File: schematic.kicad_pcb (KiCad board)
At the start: 2 copper layers, 169.7 x 127.8 mm, 108 parts, among them J3 USB_C_Receptacle_USB2.0_16P

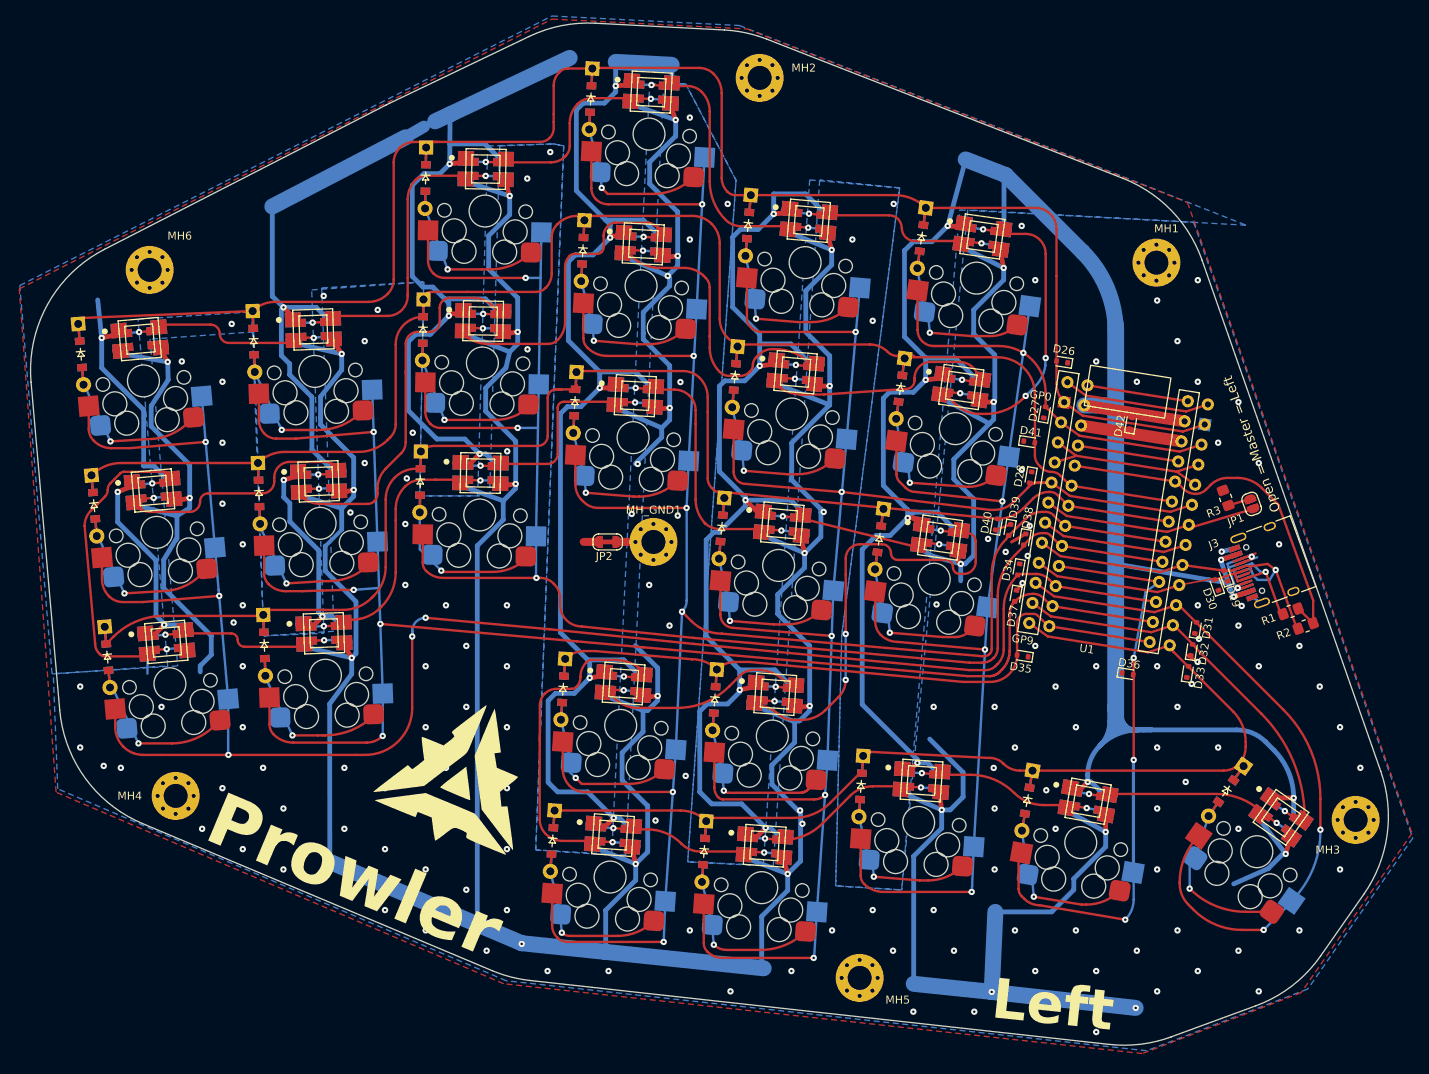
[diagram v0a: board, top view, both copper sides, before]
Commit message: Replace LEDs with reverse mount variant
Previous LEDs collided with switch
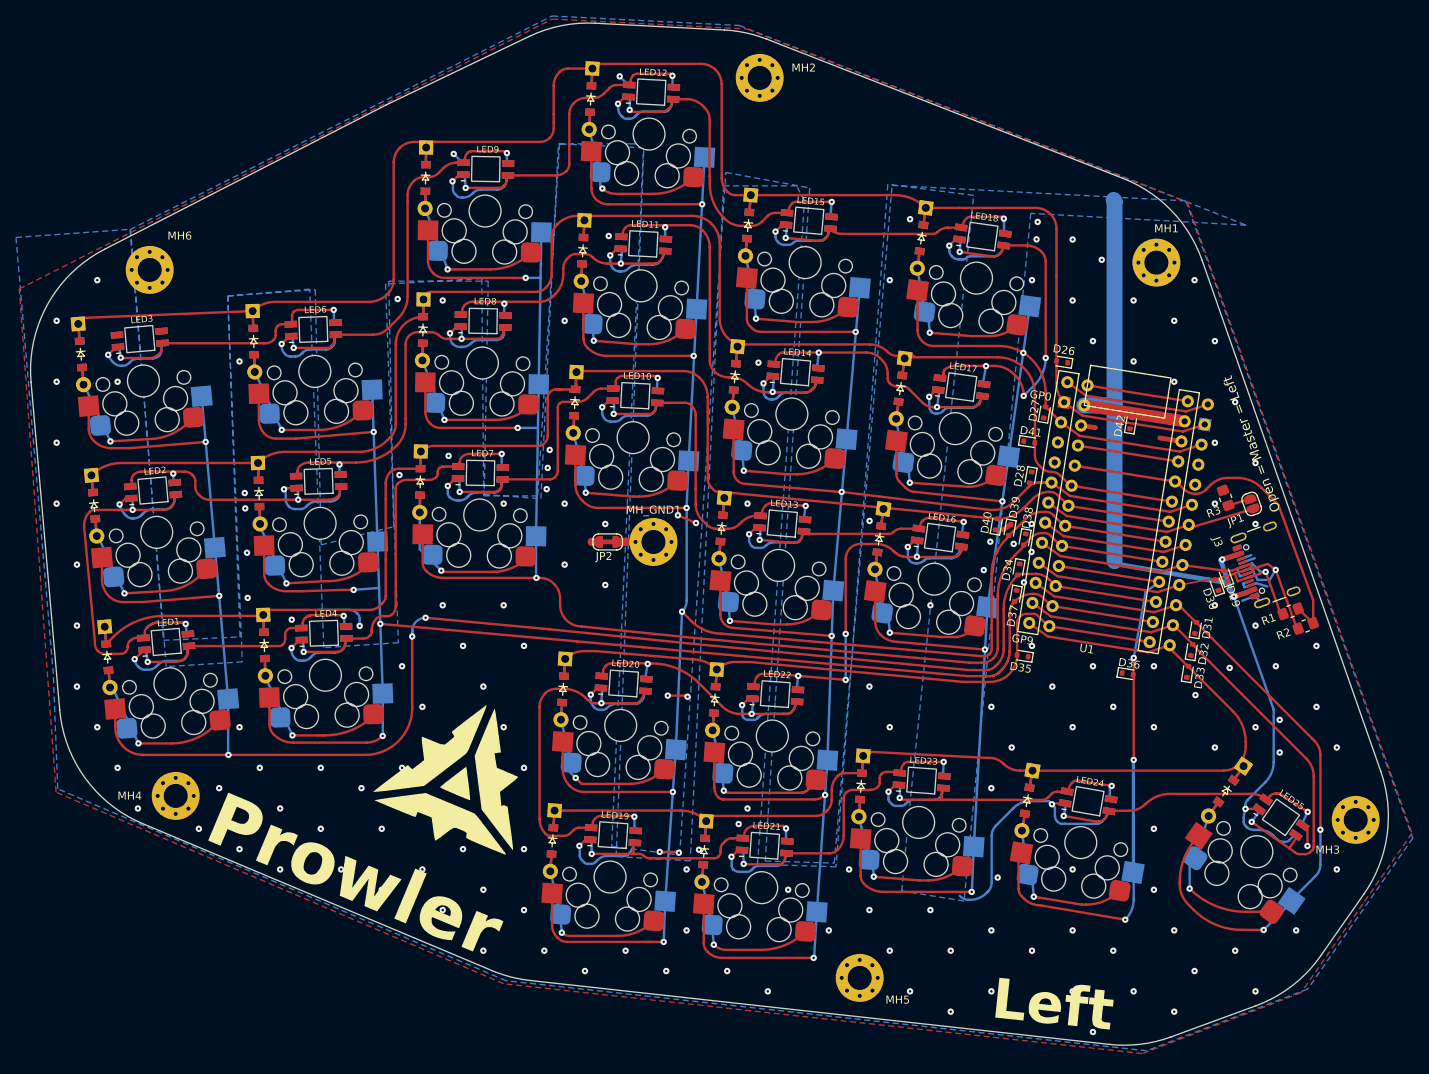
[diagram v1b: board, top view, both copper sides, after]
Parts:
- J3: footprint Connector_USB:USB_C_Receptacle_HRO_TYPE-C-31-M-12 -> Connector_USB:USB_C_Receptacle_GCT_USB4105-xx-A_16P_TopMnt_Horizontal
- LED1, LED10, LED11, LED12, LED13, LED14, LED15, LED16, LED17, LED18, LED19, LED2, LED20, LED21, LED22, LED23, LED24, LED25, LED3, LED4, LED5, LED6, LED7, LED8, LED9: value Val** -> SK6812MINI-E; footprint footprints:WS2812B -> footprints:SK6812MINI-E_RVRSMOUNT
- turned LED1 to -175 degrees
- turned LED10 to 177 degrees
- turned LED11 to 177 degrees
- turned LED12 to 177 degrees
- turned LED13 to 175 degrees
- turned LED14 to 175 degrees
- turned LED15 to 175 degrees
- turned LED16 to 172 degrees
- turned LED17 to 172 degrees
- turned LED18 to 172 degrees
- turned LED19 to 176 degrees
- turned LED2 to -175 degrees
- turned LED20 to 176 degrees
- turned LED21 to 176 degrees
- turned LED22 to 176 degrees
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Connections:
- LED3 pad 2: /NC_1 -> (no net)
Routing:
- net GND: track 880.6 -> 30.3 mm, vias 181 -> 164
- net Vraw: track 990.9 -> 426.9 mm, vias 27 -> 33
- net /LED7: track 65.2 -> 48.2 mm
- net /LED: track 52.9 -> 67.1 mm
- net /LED16: track 47.0 -> 34.6 mm
- net /LED3: track 27.1 -> 38.5 mm
- net /LED11: track 37.5 -> 48.9 mm
- net /LED15: track 56.0 -> 44.7 mm
- net /LED4: track 23.9 -> 33.5 mm
- net /LED10: track 30.7 -> 39.9 mm
- net /LED23: track 40.9 -> 48.9 mm
- net /LED22: track 32.1 -> 39.8 mm
- net /LED1: track 29.5 -> 36.5 mm
- net /LED8: track 24.0 -> 30.9 mm
- net /LED2: track 26.0 -> 32.7 mm
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
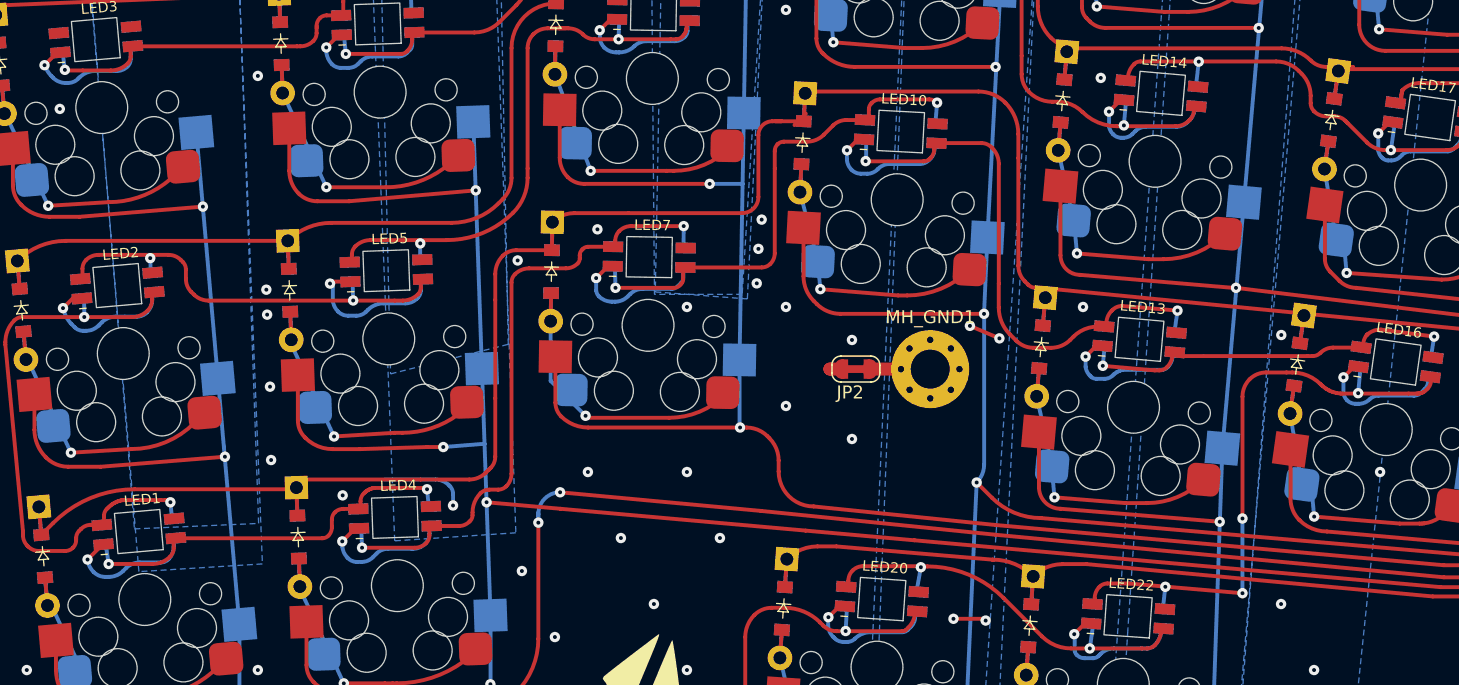
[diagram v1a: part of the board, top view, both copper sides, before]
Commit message: Add silk screen designators to reverse side
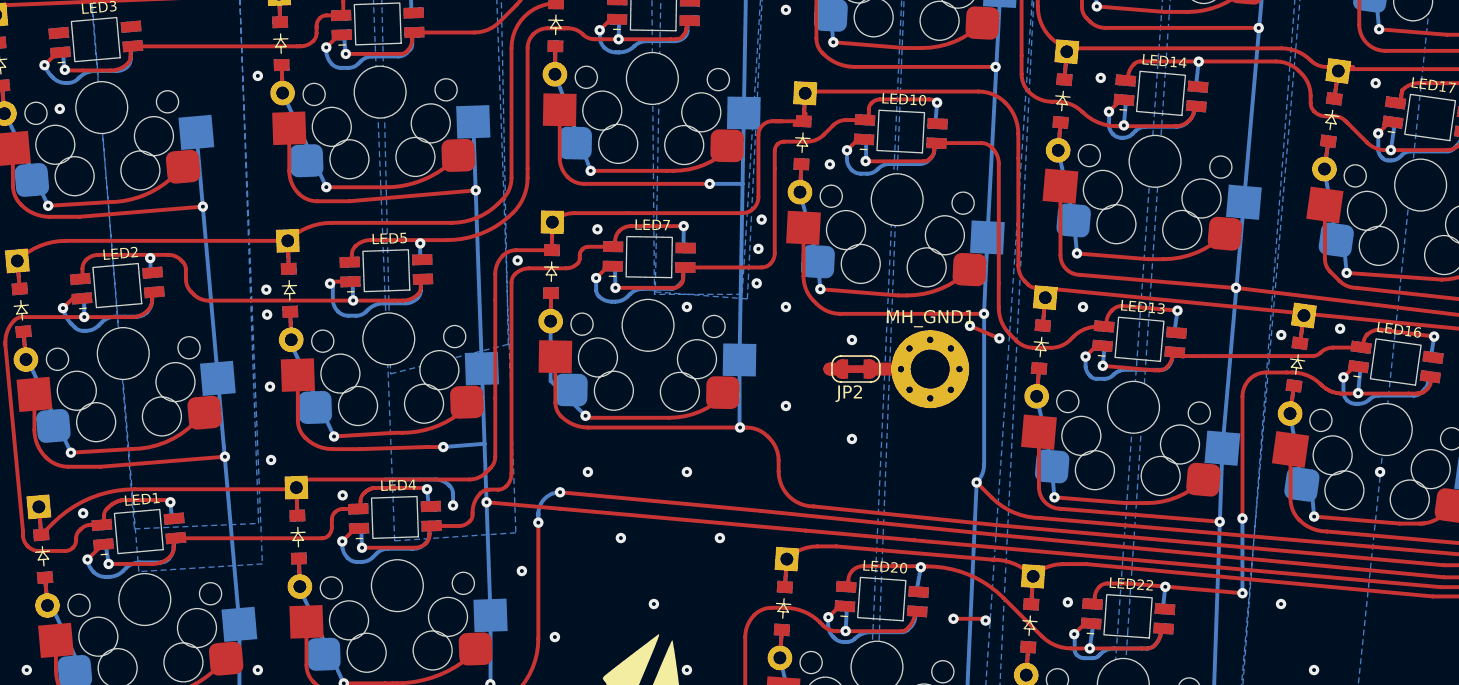
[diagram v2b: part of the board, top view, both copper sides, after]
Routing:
- net GND: vias 164 -> 169
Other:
- board text added: "J3"
- board text added: "LED1"
- board text added: "LED10"
- board text added: "LED11"
- board text added: "LED12"
- board text added: "LED13"
- board text added: "LED14"
- board text added: "LED15"
- board text added: "LED16"
- board text added: "LED17"
- board text added: "LED18"
- board text added: "LED19"
- board text added: "LED2"
- board text added: "LED20"
- board text added: "LED21"
- board text added: "LED22"
- board text added: "LED23"
- board text added: "LED24"
- board text added: "LED25"
- board text added: "LED3"
- board text added: "LED4"
- board text added: "LED5"
- board text added: "LED6"
- board text added: "LED7"
- board text added: "LED8"
- board text added: "LED9"
- board text added: "MH1"
- board text added: "MH2"
- board text added: "MH3"
- board text added: "MH4"
- board text added: "MH5"
- board text added: "MH6"
- board text added: "MH_GND1"

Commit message: Add external pullup resistors
Just in case
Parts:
- added R10: 10k, Resistor_SMD:R_0805_2012Metric_Pad1.20x1.40mm_HandSolder, B.Cu at (190.1, 130.5)
- added R11: 10k, Resistor_SMD:R_0805_2012Metric_Pad1.20x1.40mm_HandSolder, B.Cu at (191.7, 120.7)
- added R4: 10k, Resistor_SMD:R_0805_2012Metric_Pad1.20x1.40mm_HandSolder, B.Cu at (190.5, 128.2)
- added R5: 10k, Resistor_SMD:R_0805_2012Metric_Pad1.20x1.40mm_HandSolder, B.Cu at (188.5, 140.7)
- added R6: 10k, Resistor_SMD:R_0805_2012Metric_Pad1.20x1.40mm_HandSolder, B.Cu at (188.2, 142.6)
- added R7: 10k, Resistor_SMD:R_0805_2012Metric_Pad1.20x1.40mm_HandSolder, B.Cu at (188.8, 138.8)
- added R8: 10k, Resistor_SMD:R_0805_2012Metric_Pad1.20x1.40mm_HandSolder, B.Cu at (187.9, 144.6)
- added R9: 10k, Resistor_SMD:R_0805_2012Metric_Pad1.20x1.40mm_HandSolder, B.Cu at (189.2, 135.2)
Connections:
- LED3 pad 2: (no net) -> /Switch3/Dout
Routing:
- net /Vcc: track 46.1 -> 89.5 mm, vias 0 -> 1
- net /P27: track 272.3 -> 277.9 mm
- net /P23: track 205.6 -> 211.0 mm
- net /P22: track 89.7 -> 95.0 mm
- net /P20: track 242.5 -> 247.8 mm
- net /P26: track 195.0 -> 200.3 mm
- net /P1: track 181.1 -> 183.4 mm
- net /P2: track 230.6 -> 232.8 mm
- net /P7: track 89.9 -> 92.1 mm
- net GND: track 30.3 -> 28.6 mm, vias 169 -> 167
- net Vraw: track 426.9 -> 425.7 mm, vias 33 -> 35
